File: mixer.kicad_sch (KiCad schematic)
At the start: 23 parts, among them U18 RFFC5072

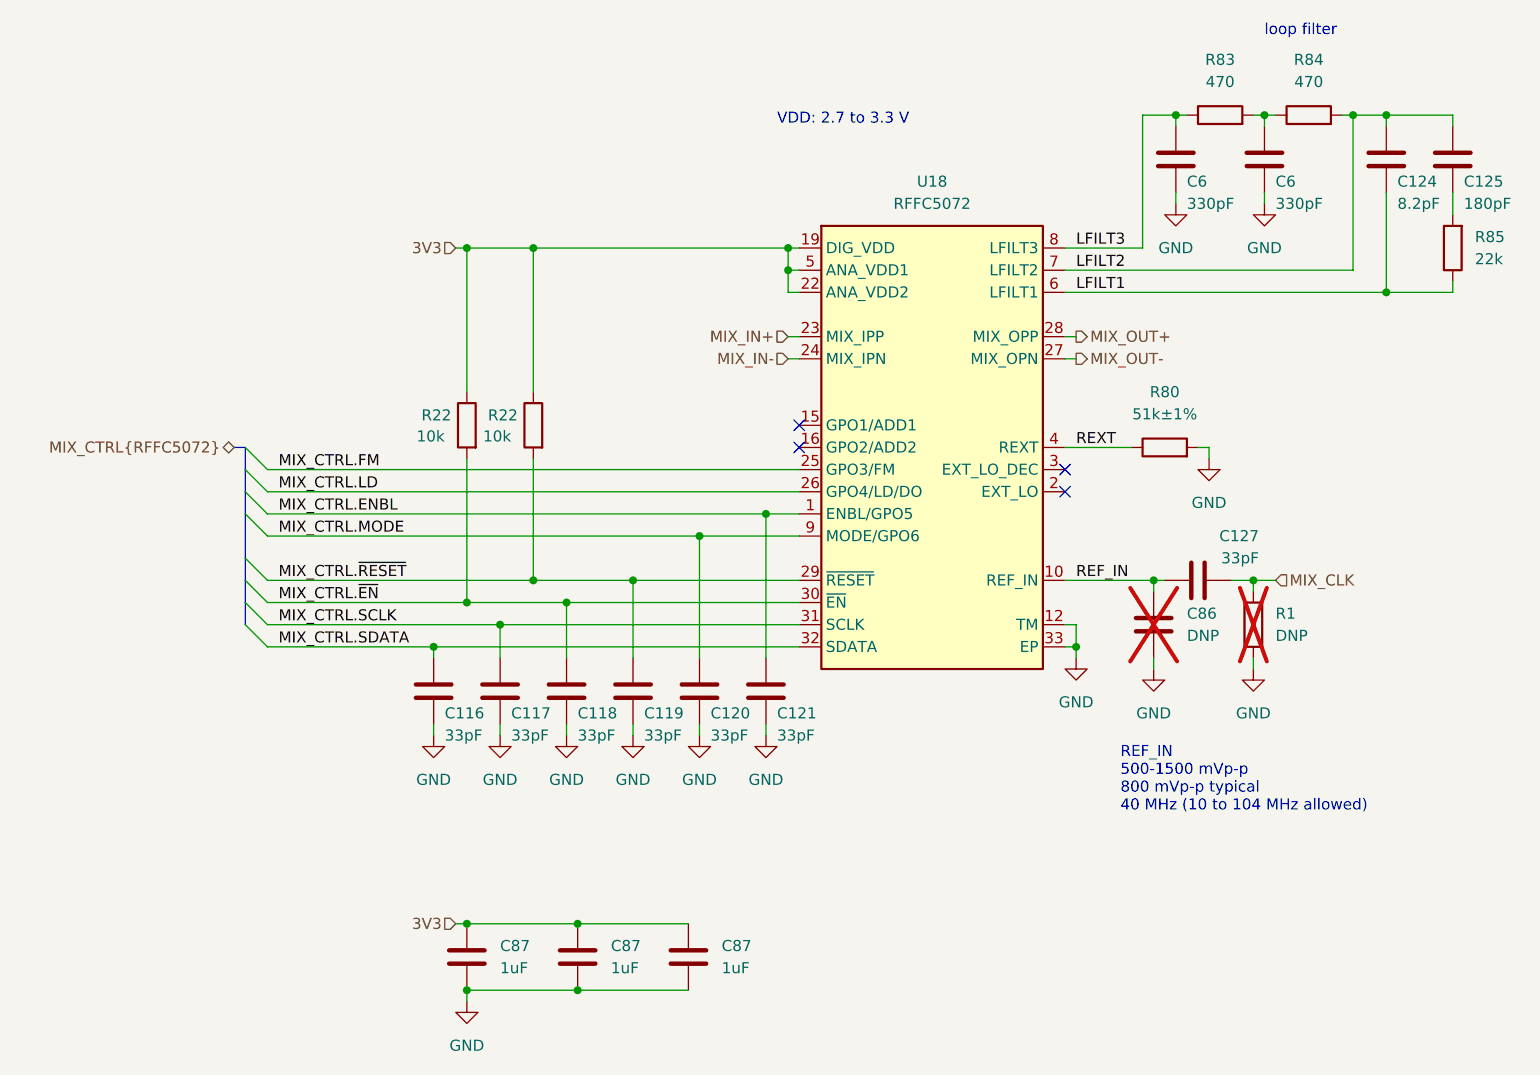
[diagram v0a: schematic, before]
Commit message: Replace open drain clock inverters with push-pull
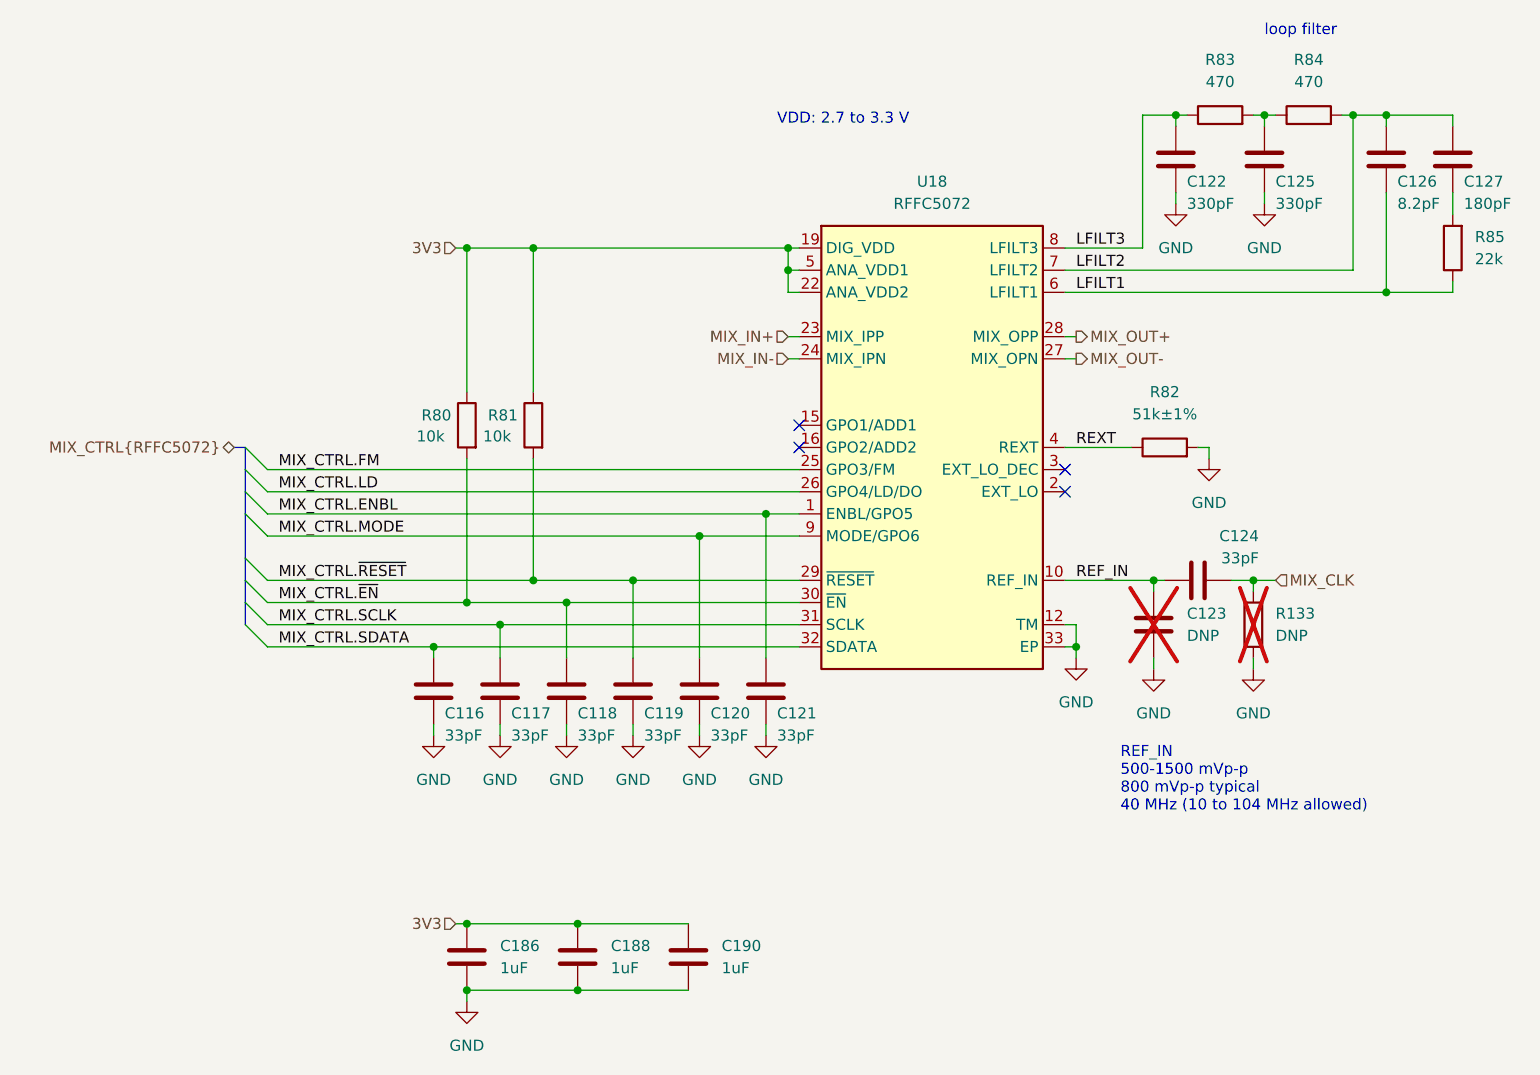
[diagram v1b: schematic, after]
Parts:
- renumbered C6 to C122, C86 to C123, C127 to C124, C6 to C125, C124 to C126, C125 to C127, C87 to C186, C87 to C188, C87 to C190, R1 to R133, R22 to R80, R22 to R81, R80 to R82

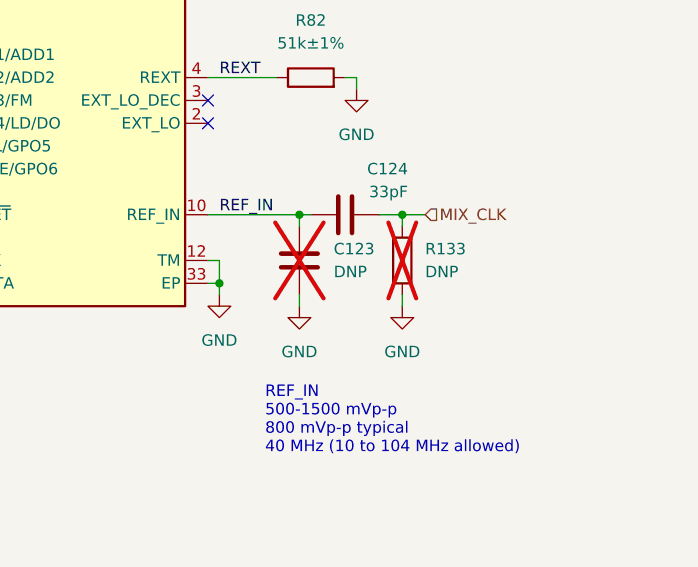
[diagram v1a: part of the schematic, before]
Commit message: Tune clock passives
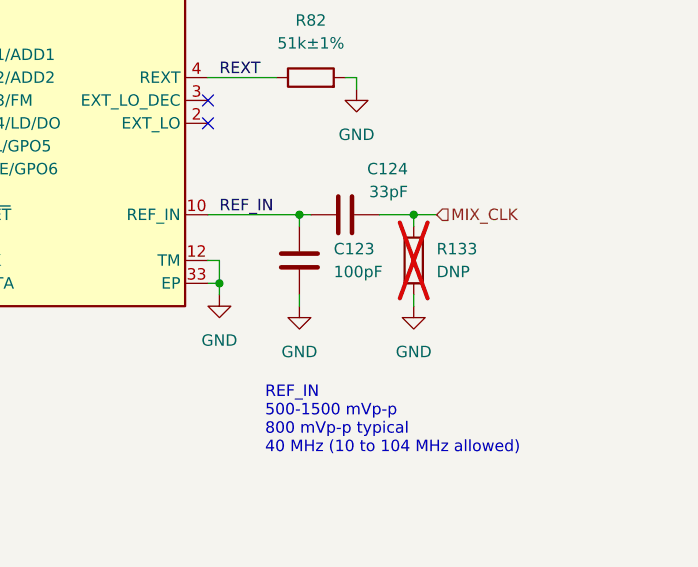
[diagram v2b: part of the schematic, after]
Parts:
- C123: value DNP -> 100pF; Manufacturer (none) -> Samsung; Part Number (none) -> CL03C101JA3NNNC; now fitted
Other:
- moved on the sheet: R133
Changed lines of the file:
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@@
   (junction (at 99.06 120.65) (diameter 0) (color 0 0 0 0)
   )
-  (junction (at 193.04 113.03) (diameter 0) (color 0 0 0 0)
+  (junction (at 194.31 113.03) (diameter 0) (color 0 0 0 0)
   )
   (junction (at 139.7 77.47) (diameter 0) (color 0 0 0 0)
@@
     (stroke (width 0) (type default))
   )
-  (wire (pts (xy 193.04 113.03) (xy 193.04 114.3))
+  (wire (pts (xy 194.31 113.03) (xy 194.31 114.3))
     (stroke (width 0) (type default))
   )
@@
     (stroke (width 0) (type default))
   )
-  (wire (pts (xy 193.04 113.03) (xy 195.58 113.03))
+  (wire (pts (xy 194.31 113.03) (xy 196.85 113.03))
     (stroke (width 0) (type default))
   )
@@
     (stroke (width 0) (type default))
   )
-  (wire (pts (xy 193.04 121.92) (xy 193.04 123.19))
+  (wire (pts (xy 194.31 121.92) (xy 194.31 123.19))
     (stroke (width 0) (type default))
   )
@@
     (stroke (width 0) (type default))
   )
-  (wire (pts (xy 190.5 113.03) (xy 193.04 113.03))
+  (wire (pts (xy 190.5 113.03) (xy 194.31 113.03))
     (stroke (width 0) (type default))
   )
@@
     (effects (font (size 1.27 1.27)) (justify left))
   )
-  (hierarchical_label "MIX_CLK" (shape input) (at 195.58 113.03 0) (fields_autoplaced)
+  (hierarchical_label "MIX_CLK" (shape input) (at 196.85 113.03 0) (fields_autoplaced)
     (effects (font (size 1.27 1.27)) (justify left))
   )
@@
     )
   )
-  (symbol (lib_id "power:GND") (at 193.04 123.19 0) (unit 1)
-    (in_bom yes) (on_board yes) (dnp no) (fields_autoplaced)
-    (property "Reference" "#PWR0342" (at 193.04 129.54 0)
-      (effects (font (size 1.27 1.27)) hide)
-    )
-    (property "Value" "GND" (at 193.04 128.27 0)
-      (effects (font (size 1.27 1.27)))
-    )
-    (property "Footprint" "" (at 193.04 123.19 0)
-      (effects (font (size 1.27 1.27)) hide)
-    )
-    (property "Datasheet" "" (at 193.04 123.19 0)
+  (symbol (lib_id "power:GND") (at 194.31 123.19 0) (unit 1)
+    (in_bom yes) (on_board yes) (dnp no) (fields_autoplaced)
+    (property "Reference" "#PWR0342" (at 194.31 129.54 0)
+      (effects (font (size 1.27 1.27)) hide)
+    )
+    (property "Value" "GND" (at 194.31 128.27 0)
+      (effects (font (size 1.27 1.27)))
+    )
+    (property "Footprint" "" (at 194.31 123.19 0)
+      (effects (font (size 1.27 1.27)) hide)
+    )
+    (property "Datasheet" "" (at 194.31 123.19 0)
       (effects (font (size 1.27 1.27)) hide)
     )
@@
     )
   )
-  (symbol (lib_id "Device:R") (at 193.04 118.11 0) (unit 1)
+  (symbol (lib_id "Device:R") (at 194.31 118.11 0) (unit 1)
     (in_bom yes) (on_board yes) (dnp yes) (fields_autoplaced)
-    (property "Reference" "R133" (at 195.58 116.84 0)
-      (effects (font (size 1.27 1.27)) (justify left))
-    )
-    (property "Value" "DNP" (at 195.58 119.38 0)
-      (effects (font (size 1.27 1.27)) (justify left))
-    )
-    (property "Footprint" "Resistor_SMD:R_0402_1005Metric" (at 191.262 118.11 90)
-      (effects (font (size 1.27 1.27)) hide)
-    )
-    (property "Datasheet" "~" (at 193.04 118.11 0)
-      (effects (font (size 1.27 1.27)) hide)
-    )
-    (property "Part Number" "" (at 193.04 118.11 0)
-      (effects (font (size 1.27 1.27)) hide)
-    )
-    (property "Substitution" "" (at 193.04 118.11 0)
-      (effects (font (size 1.27 1.27)) hide)
-    )
-    (property "Description" "" (at 193.04 118.11 0)
-      (effects (font (size 1.27 1.27)) hide)
-    )
-    (property "Manufacturer" "" (at 193.04 118.11 0)
+    (property "Reference" "R133" (at 196.85 116.84 0)
+      (effects (font (size 1.27 1.27)) (justify left))
+    )
+    (property "Value" "DNP" (at 196.85 119.38 0)
+      (effects (font (size 1.27 1.27)) (justify left))
+    )
+    (property "Footprint" "Resistor_SMD:R_0402_1005Metric" (at 192.532 118.11 90)
+      (effects (font (size 1.27 1.27)) hide)
+    )
+    (property "Datasheet" "~" (at 194.31 118.11 0)
+      (effects (font (size 1.27 1.27)) hide)
+    )
+    (property "Part Number" "" (at 194.31 118.11 0)
+      (effects (font (size 1.27 1.27)) hide)
+    )
+    (property "Substitution" "" (at 194.31 118.11 0)
+      (effects (font (size 1.27 1.27)) hide)
+    )
+    (property "Description" "" (at 194.31 118.11 0)
+      (effects (font (size 1.27 1.27)) hide)
+    )
+    (property "Manufacturer" "" (at 194.31 118.11 0)
       (effects (font (size 1.27 1.27)) hide)
     )
@@
   )
   (symbol (lib_id "Device:C") (at 181.61 118.11 0) (unit 1)
-    (in_bom yes) (on_board yes) (dnp yes) (fields_autoplaced)
+    (in_bom yes) (on_board yes) (dnp no) (fields_autoplaced)
     (property "Reference" "C123" (at 185.42 116.84 0)
       (effects (font (size 1.27 1.27)) (justify left))
     )
-    (property "Value" "DNP" (at 185.42 119.38 0)
+    (property "Value" "100pF" (at 185.42 119.38 0)
       (effects (font (size 1.27 1.27)) (justify left))
     )
@@
       (effects (font (size 1.27 1.27)) hide)
     )
+    (property "Description" "CAP CER 100PF 25V C0G/NP0 0201" (at 181.61 118.11 0)
+      (effects (font (size 1.27 1.27)) hide)
+    )
+    (property "Manufacturer" "Samsung" (at 181.61 118.11 0)
+      (effects (font (size 1.27 1.27)) hide)
+    )
+    (property "Part Number" "CL03C101JA3NNNC" (at 181.61 118.11 0)
+      (effects (font (size 1.27 1.27)) hide)
+    )
+    (property "Substitution" "" (at 181.61 118.11 0)
+      (effects (font (size 1.27 1.27)) hide)
+    )
